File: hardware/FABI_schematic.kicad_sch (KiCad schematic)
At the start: 63 parts, among them J1 Conn_01x02_Pin, J11_GND1 Conn_01x01_Male, J11_VDD1 Conn_01x01_Male, J11_data1 Conn_01x01_Male, J12 Conn_01x04_Socket, J2 display_connector_91601-304LF, J3 54601-906WPLF, J4 54-00174 / FC68125, J5 54-00174 / FC68125, J6 009159005551906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

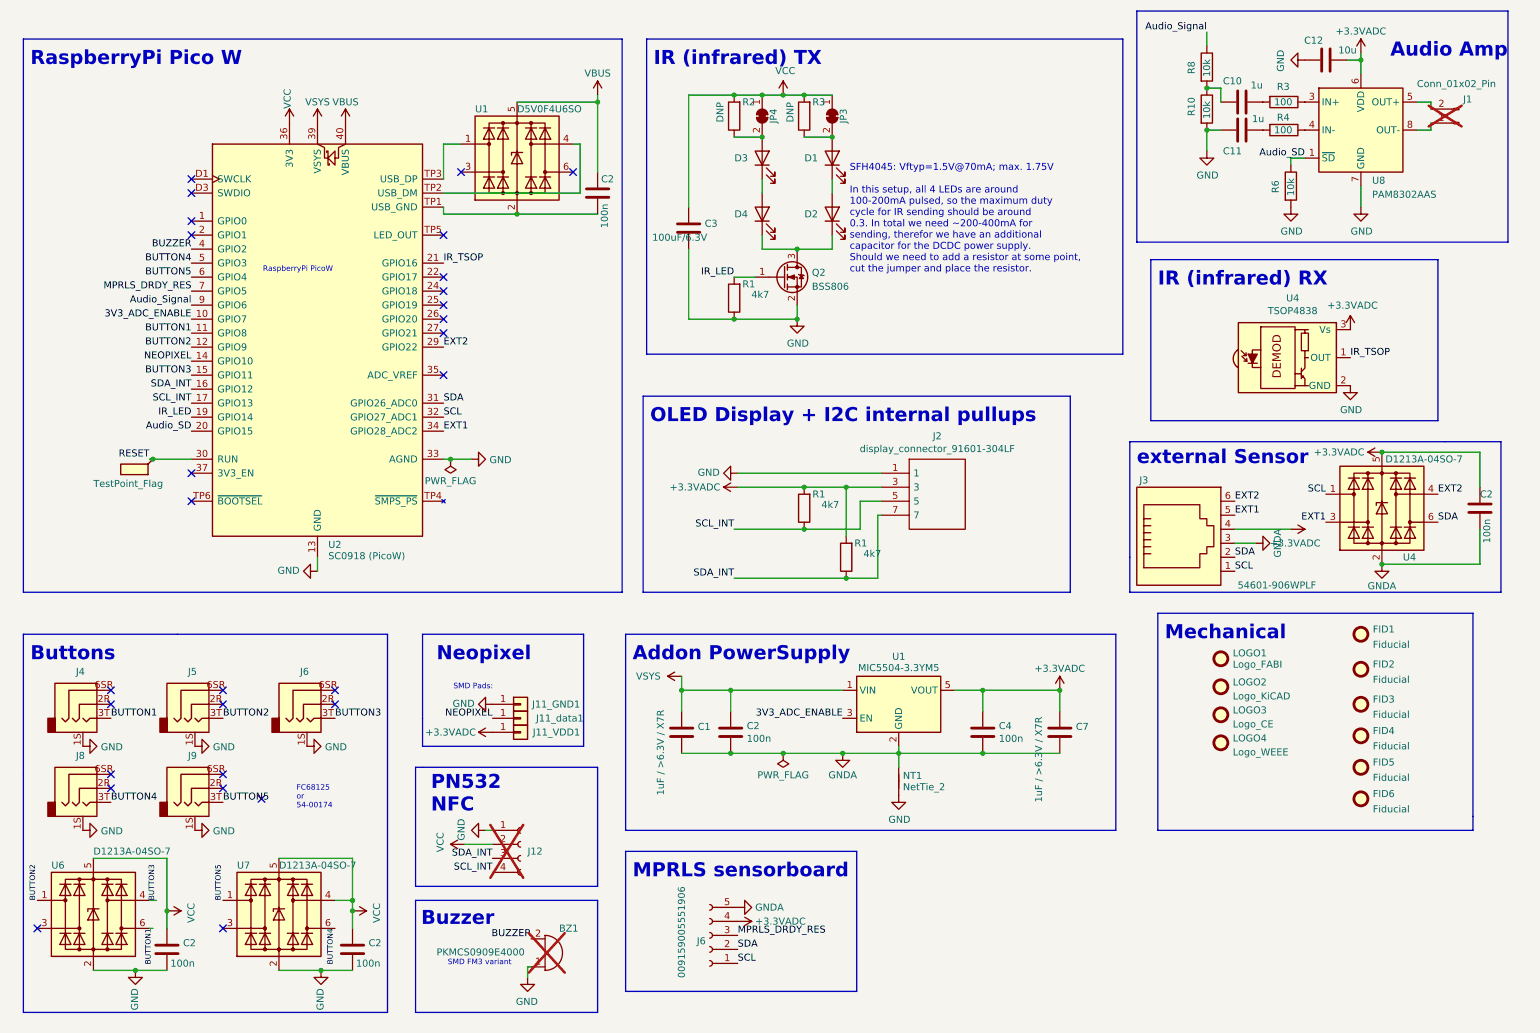
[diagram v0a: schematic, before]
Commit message: Added all prev. modifications to SRC_v3.0 update by ChrisVeigl; Removed redundant LDO; Most components of the BMS is on the board except for testpoints and battery measurement resistors; Wired most components;
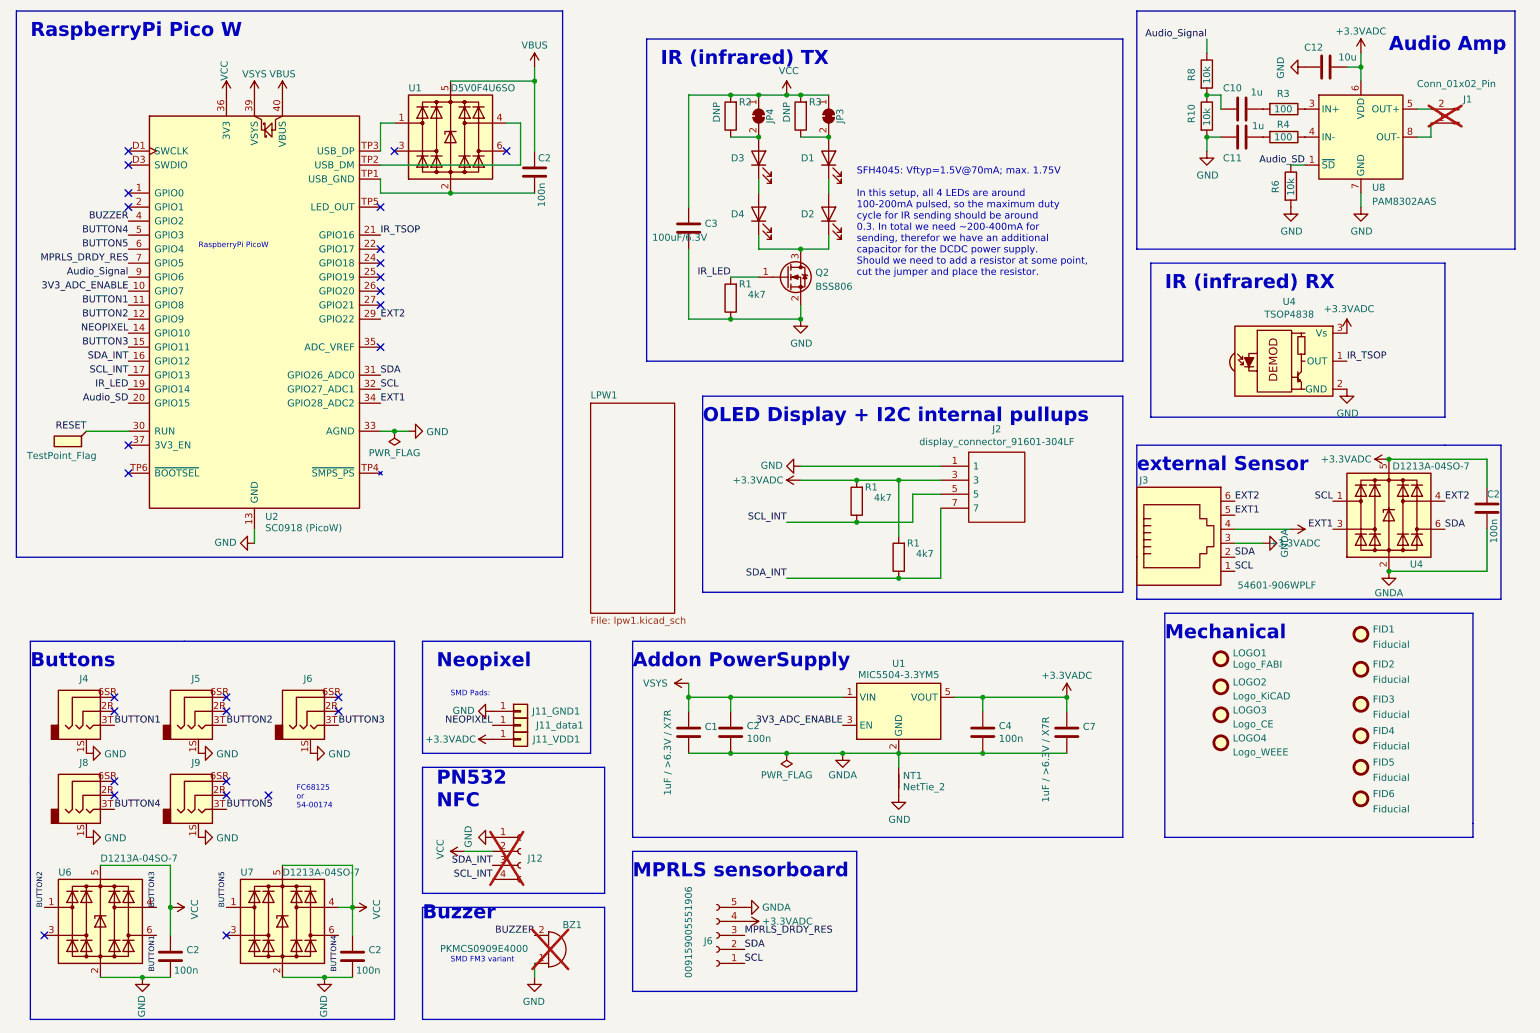
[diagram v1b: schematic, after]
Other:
- added sheet LPW1 (lpw1.kicad_sch)
- moved on the sheet: BZ1, C1, C10, C11, C12, C2, C7, D1, D2, D3, D4, J11_GND1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

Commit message: Added solder jumper between BAT and p-MOS; Rewired battery level measurem. to GPIO pin in order to have it off when not needed; Changed all Rs into EU Rs; Renamed all components for them to be uniform; Removed Schottky since Pico W has its own built in as well as pulldown R; Changed p-MOSFET to recommended p-MOS in 28 page datasheet (Pico W); Changed Footprint of Audio AMP, rewired too;
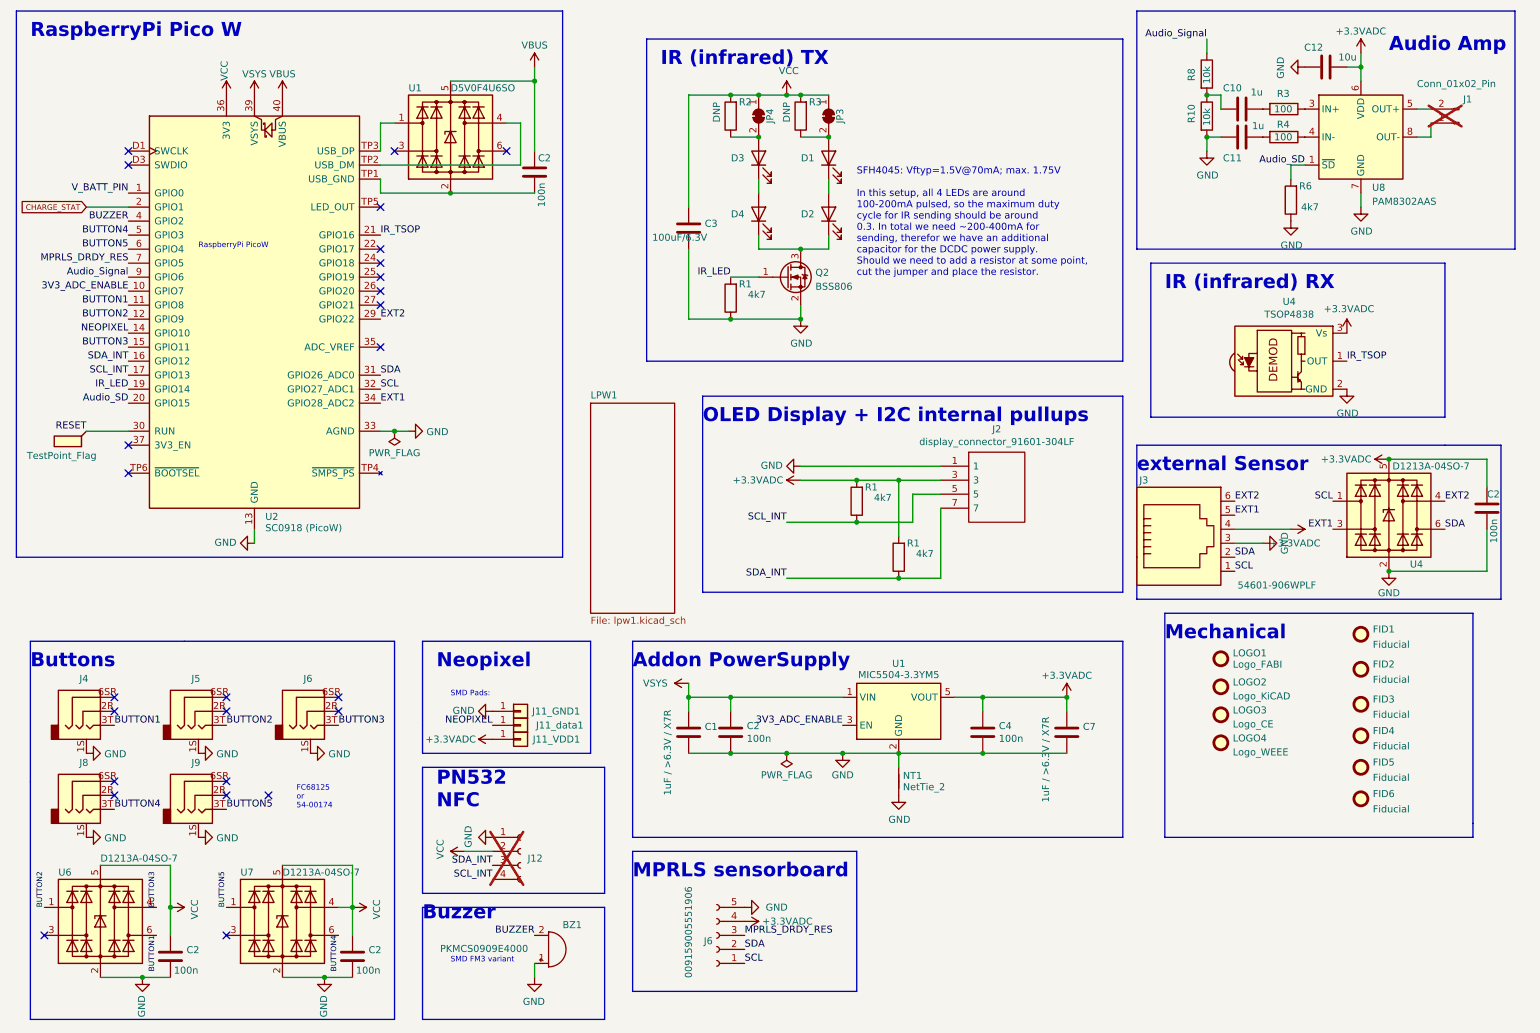
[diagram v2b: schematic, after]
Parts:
- BZ1: now fitted
- R6: value 10k -> 4k7; Digikey 541-2204-1-ND -> 1292-WR06X472JTLCT-ND; Farnell 2616584 -> 3994558; Mouser 71-RCA060310K0FKEA -> 756-WCR0603-4K7FI; RS Components 188-5836 -> 199-5594
- U1: Farnell (none) -> 3127271; Mouser (none) -> 621-D5V0F4U6SO-7
- U8: footprint Package_SO:MSOP-8_3x3mm_P0.65mm -> Package_SO:SOIC-8_3.9x4.9mm_P1.27mm
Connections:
- net GNDA is gone; now on net GND: C1.2, C2.2, C2.2, C4.2, C7.2, J3.3, J6.5 (Pin_5), NT1.2, U1.2 (GND), U4.2 (GND)
- net Audio_SD: now also R6.2; no longer R6.1
- net GND: now also R6.1; no longer R6.2
- net V_BATT_PIN: now reaches U2.1 (GPIO0)
- net CHARGE_STAT: now reaches U2.2 (GPIO1)
- no-connect marks 28 -> 26
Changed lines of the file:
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@@
 	)
 	(no_connect
-		(at 33.02 50.8)
-	)
-	(no_connect
 		(at 78.74 66.04)
 	)
@@
 	)
 	(no_connect
-		(at 33.02 48.26)
-	)
-	(no_connect
 		(at 30.48 139.7)
 	)
@@
 	(wire
 		(pts
+			(xy 25.4 50.8) (xy 33.02 50.8)
+		)
+		(stroke
+			(width 0)
+			(type default)
+		)
+	)
+	(wire
+		(pts
 			(xy 182.88 139.7) (xy 187.96 139.7)
 		)
@@
 		)
 	)
+	(wire
+		(pts
+			(xy 243.84 43.18) (xy 243.84 45.72)
+		)
+		(stroke
+			(width 0)
+			(type default)
+		)
+	)
 	(polyline
 		(pts
@@
 		)
 	)
+	(label "V_BATT_PIN"
+		(at 33.02 48.26 180)
+		(fields_autoplaced yes)
+		(effects
+			(font
+				(size 1.27 1.27)
+			)
+			(justify right bottom)
+		)
+	)
 	(label "NEOPIXEL"
 		(at 99.06 144.78 180)
@@
 		)
 	)
+	(global_label "CHARGE_STAT"
+		(shape input)
+		(at 25.4 50.8 180)
+		(fields_autoplaced yes)
+		(effects
+			(font
+				(size 0.9906 0.9906)
+			)
+			(justify right)
+		)
+		(property "Intersheetrefs" "${INTERSHEET_REFS}"
+			(at 13.7704 50.8 0)
+			(effects
+				(font
+					(size 1.27 1.27)
+				)
+				(justify right)
+				(hide yes)
+			)
+		)
+	)
 	(symbol
 		(lib_id "power:GND")
@@
 			)
 		)
-		(property "Value" "GNDA"
-			(at 147.955 177.8 90)
+		(property "Value" "GND"
+			(at 148.59 177.7999 90)
 			(effects
 				(font
@@
 			)
 		)
-		(property "Footprint" "Package_SO:MSOP-8_3x3mm_P0.65mm"
+		(property "Footprint" "Package_SO:SOIC-8_3.9x4.9mm_P1.27mm"
 			(at 256.54 38.1 0)
 			(effects
@@
 			)
 		)
-		(property "Value" "GNDA"
+		(property "Value" "GND"
 			(at 162.56 153.805 0)
 			(effects
@@
 			)
 		)
-		(property "Value" "GNDA"
+		(property "Value" "GND"
 			(at 242.705 111.76 0)
 			(effects
@@
 		(in_bom yes)
 		(on_board yes)
-		(dnp yes)
+		(dnp no)
 		(property "Reference" "BZ1"
 			(at 111.76 180.975 0)
@@
 	(symbol
 		(lib_id "power:GND")
-		(at 243.84 50.8 0)
+		(at 243.84 53.34 0)
 		(unit 1)
 		(exclude_from_sim no)
@@
 		(dnp no)
 		(property "Reference" "#PWR08"
-			(at 243.84 57.15 0)
+			(at 243.84 59.69 0)
 			(effects
 				(font
@@
 		)
 		(property "Value" "GND"
-			(at 243.967 55.1942 0)
+			(at 243.967 57.7342 0)
 			(effects
 				(font
@@
 		)
 		(property "Footprint" ""
-			(at 243.84 50.8 0)
+			(at 243.84 53.34 0)
 			(effects
 				(font
@@
 		)
 		(property "Datasheet" ""
-			(at 243.84 50.8 0)
+			(at 243.84 53.34 0)
 			(effects
 				(font
@@
 		)
 		(property "Description" ""
-			(at 243.84 50.8 0)
+			(at 243.84 53.34 0)
 			(effects
 				(font
@@
 			)
 		)
-		(property "Value" "GNDA"
+		(property "Value" "GND"
 			(at 261.62 120.785 0)
 			(effects
@@
 	)
 	(symbol
-		(lib_id "Device:R")
-		(at 243.84 46.99 0)
-		(unit 1)
-		(exclude_from_sim no)
-		(in_bom yes)
-		(on_board yes)
-		(dnp no)
-		(property "Reference" "R6"
-			(at 241.046 48.26 90)
-			(effects
-				(font
-					(size 1.27 1.27)
-				)
-				(justify left)
-			)
-		)
-		(property "Value" "10k"
-			(at 243.84 48.768 90)
-			(effects
-				(font
-					(size 1.27 1.27)
-				)
-				(justify left)
-			)
-		)
-		(property "Footprint" "Resistor_SMD:R_0603_1608Metric"
-			(at 242.062 46.99 90)
-			(effects
-				(font
-					(size 1.27 1.27)
-				)
-				(hide yes)
-			)
-		)
-		(property "Datasheet" "~"
-			(at 243.84 46.99 0)
-			(effects
-				(font
-					(size 1.27 1.27)
-				)
-				(hide yes)
-			)
-		)
-		(property "Description" ""
-			(at 243.84 46.99 0)
-			(effects
-				(font
-					(size 1.27 1.27)
-				)
-				(hide yes)
-			)
-		)
-		(property "Farnell" "2616584"
-			(at 243.84 46.99 0)
-			(effects
-				(font
-					(size 1.27 1.27)
-				)
-				(hide yes)
-			)
-		)
-		(property "Digikey" "541-2204-1-ND"
-			(at 243.84 46.99 0)
-			(effects
-				(font
-					(size 1.27 1.27)
-				)
-				(hide yes)
-			)
-		)
-		(property "RS Components" "188-5836 "
-			(at 243.84 46.99 0)
-			(effects
-				(font
-					(size 1.27 1.27)
-				)
-				(hide yes)
-			)
-		)
-		(property "Mouser" "71-RCA060310K0FKEA"
-			(at 243.84 46.99 0)
-			(effects
-				(font
-					(size 1.27 1.27)
-				)
-				(hide yes)
-			)
-		)
-		(pin "1"
-		)
-		(pin "2"
-		)
-		(instances
-			(project "FABI_schematic"
-				(path "/8404dabe-a0ce-44ce-a3c9-f9e9e54d2b02"
-					(reference "R6")
-					(unit 1)
-				)
-			)
-		)
-	)
-	(symbol
 		(lib_id "Device:LED")
 		(at 147.32 52.07 90)
@@
 	)
 	(symbol
+		(lib_id "Device:R")
+		(at 243.84 49.53 180)
+		(unit 1)
+		(exclude_from_sim no)
+		(in_bom yes)
+		(on_board yes)
+		(dnp no)
+		(property "Reference" "R6"
+			(at 247.65 46.99 0)
+			(effects
+				(font
+					(size 1.27 1.27)
+				)
+				(justify left)
+			)
+		)
+		(property "Value" "4k7"
+			(at 248.92 50.8 0)
+			(effects
+				(font
+					(size 1.27 1.27)
+				)
+				(justify left)
+			)
+		)
+		(property "Footprint" "Resistor_SMD:R_0603_1608Metric"
+			(at 245.618 49.53 90)
+			(effects
+				(font
+					(size 1.27 1.27)
+				)
+				(hide yes)
+			)
+		)
+		(property "Datasheet" "~"
+			(at 243.84 49.53 0)
+			(effects
+				(font
+					(size 1.27 1.27)
+				)
+				(hide yes)
+			)
+		)
+		(property "Description" ""
+			(at 243.84 49.53 0)
+			(effects
+				(font
+					(size 1.27 1.27)
+				)
+				(hide yes)
+			)
+		)
+		(property "Farnell" "3994558"
+			(at 243.84 49.53 0)
+			(effects
+				(font
+					(size 1.27 1.27)
+				)
+				(hide yes)
+			)
+		)
+		(property "Digikey" "1292-WR06X472JTLCT-ND"
+			(at 243.84 49.53 0)
+			(effects
+				(font
+					(size 1.27 1.27)
+				)
+				(hide yes)
+			)
+		)
+		(property "RS Components" "199-5594"
+			(at 243.84 49.53 0)
+			(effects
+				(font
+					(size 1.27 1.27)
+				)
+				(hide yes)
+			)
+		)
+		(property "Mouser" "756-WCR0603-4K7FI"
+			(at 243.84 49.53 0)
+			(effects
+				(font
+					(size 1.27 1.27)
+				)
+				(hide yes)
+			)
+		)
+		(pin "1"
+		)
+		(pin "2"
+		)
+		(instances
+			(project "FABI_schematic"
+				(path "/8404dabe-a0ce-44ce-a3c9-f9e9e54d2b02"
+					(reference "R6")
+					(unit 1)
+				)
+			)
+		)
+	)
+	(symbol
 		(lib_id "FABI_customLib:AudioJack3_Ground")
 		(at 25.4 157.48 0)
@@
 				)
 				(hide yes)
+			)
+		)
+		(property "Farnell" "3127271 "
+			(at 91.44 38.1 0)
+			(effects
+				(font
+					(size 0.9906 0.9906)
+				)
+				(hide yes)
+			)
+		)
+		(property "Mouser" "621-D5V0F4U6SO-7"
+			(at 91.44 38.1 0)
+			(effects
+				(font
+					(size 0.9906 0.9906)
+				)
+				(hide yes)
+			)
+		)
+		(property "RS comp" ""
+			(at 91.44 38.1 0)
+			(effects
+				(font
+					(size 0.9906 0.9906)
+				)
+				(hide yes)

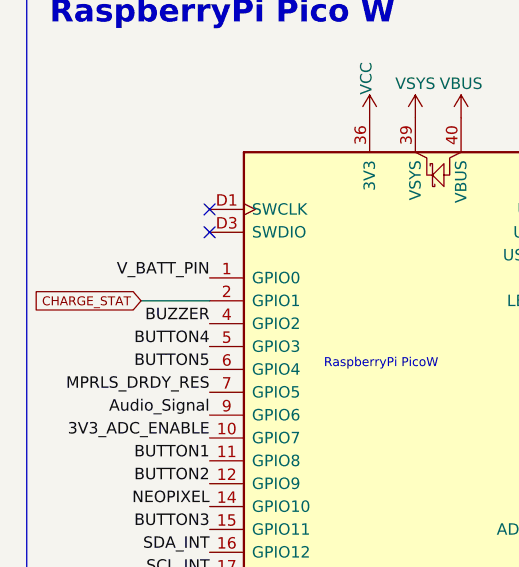
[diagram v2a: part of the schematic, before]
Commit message: Done more finetuning; No more ADC Pin on the Pico W left, waiting for response/recommendation of prof.; Made sure that every route is correct; Added new GPIO inputs, namely voltage divider so it would not constantly draw current (V_BATT_VD_SWITCH), (CHARGE_STAT) from the MCP STAT pin;
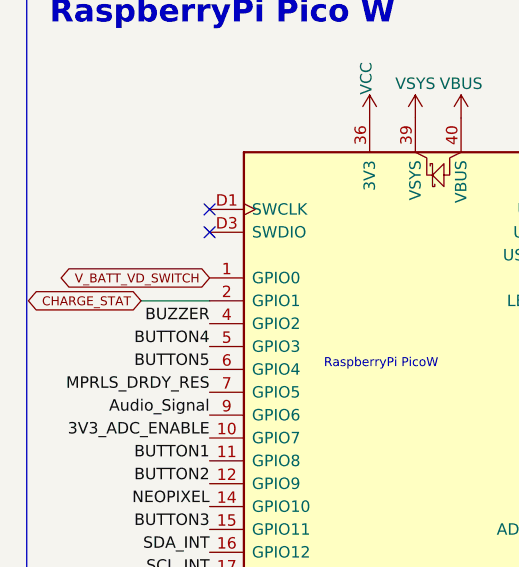
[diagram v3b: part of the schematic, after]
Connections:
- net V_BATT_PIN renamed V_BATT_VD_SWITCH
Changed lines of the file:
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@@
-		)
-	)
-	(label "V_BATT_PIN"
-		(at 33.02 48.26 180)
-		(fields_autoplaced yes)
-		(effects
-			(font
-				(size 1.27 1.27)
-			)
-			(justify right bottom)
 		)
 	)
@@
 	)
 	(global_label "CHARGE_STAT"
-		(shape input)
+		(shape bidirectional)
 		(at 25.4 50.8 180)
 		(fields_autoplaced yes)
@@
 		)
 		(property "Intersheetrefs" "${INTERSHEET_REFS}"
-			(at 13.7704 50.8 0)
+			(at 13.0274 50.8 0)
 			(effects
 				(font
+					(size 1.27 1.27)
+				)
+				(justify right)
+				(hide yes)
+			)
+		)
+	)
+	(global_label "V_BATT_VD_SWITCH"
+		(shape bidirectional)
+		(at 33.02 48.26 180)
+		(fields_autoplaced yes)
+		(effects
+			(font
+				(size 0.9906 0.9906)
+			)
+			(justify right)
+		)
+		(property "Intersheetrefs" "${INTERSHEET_REFS}"
+			(at 16.8267 48.26 0)
+			(effects
+				(font
